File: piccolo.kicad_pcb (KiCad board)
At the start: 2 copper layers, 21 x 51 mm, 44 parts, among them J0 CON_PICO_40W, J1 USB_C_Receptacle_USB2.0, J2 Debug, Q1 DMG1012T, SW1 BOOTSEL, U1 RP2040, U2 ME6217C33M5, U3 MX25R1635FZUIL0, X1 SIT1602AI-22-33E-12.000000D

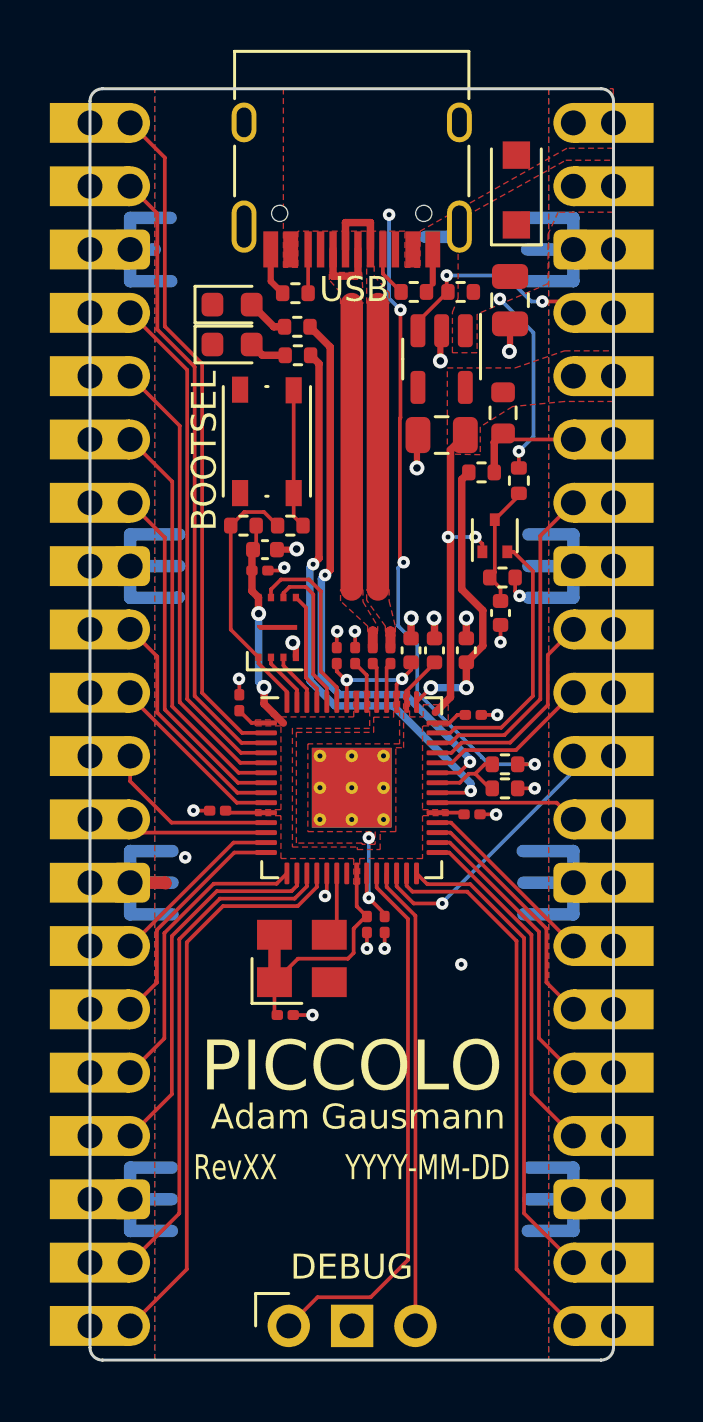
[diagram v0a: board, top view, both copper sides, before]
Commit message: value-engineered for jlcpcb
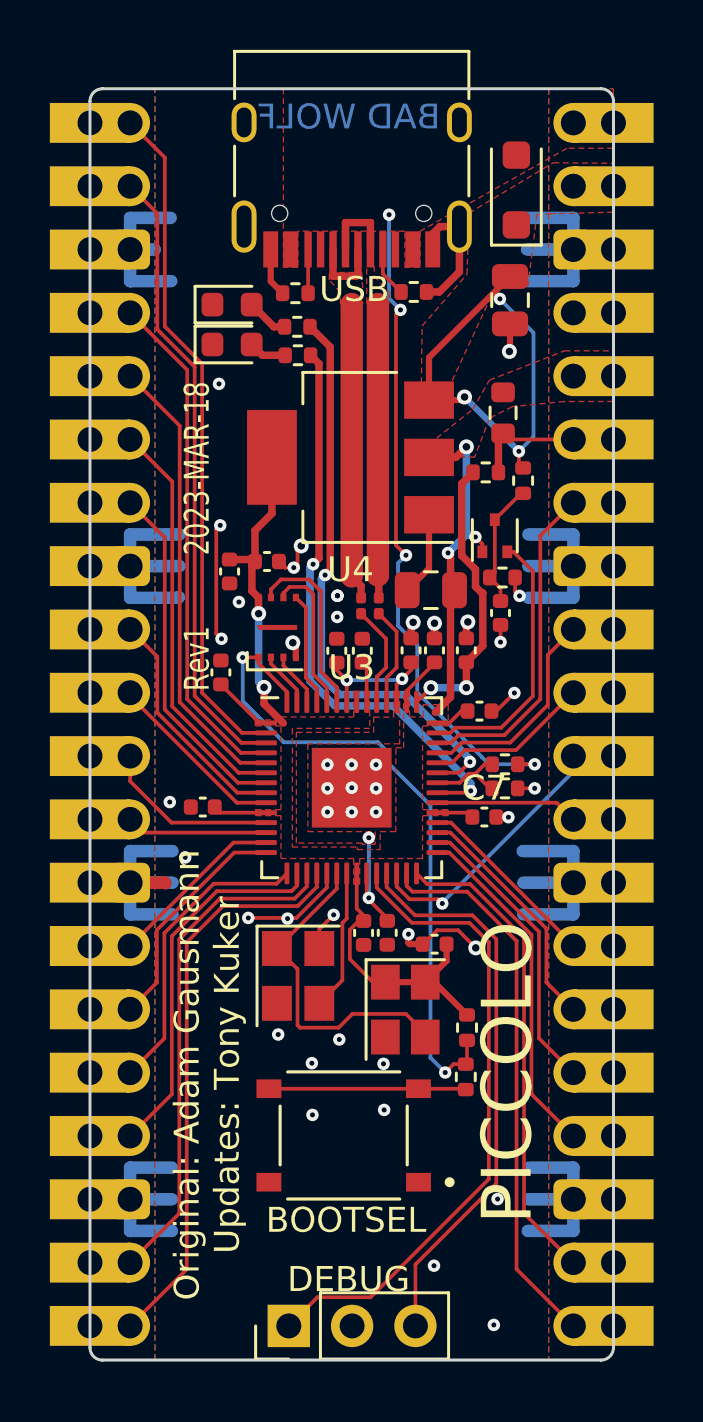
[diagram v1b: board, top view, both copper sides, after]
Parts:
- removed the R2 at (126.0, 48.4)
- removed SW1: BOOTSEL, Button_Switch_SMD:SW_Push_1P1T_NO_Vertical_Wuerth_434133025816
- removed U2: ME6217C33M5, Package_TO_SOT_SMD:SOT-23-5
- added SW2: TS-1187A-B-A-B, TS-1187A-B-A-B:SW_TS-1187A-B-A-B, F.Cu at (121.3, 82.2)
- added U4: AMS1117-3.3, Package_TO_SOT_SMD:SOT-223-3_TabPin2, F.Cu at (121.5, 55.0)
- added Y1: 12MHz, Crystal:Crystal_SMD_3225-4Pin_3.2x2.5mm, F.Cu at (119.5, 75.8)
- C10: renamed from C8; footprint Capacitor_SMD:C_0201_0603Metric -> Capacitor_SMD:C_0402_1005Metric
- C11: renamed from C10; footprint Capacitor_SMD:C_0201_0603Metric -> Capacitor_SMD:C_0402_1005Metric
- C13: renamed from C9; footprint Capacitor_SMD:C_0201_0603Metric -> Capacitor_SMD:C_0402_1005Metric
- C15: renamed from C11; footprint Capacitor_SMD:C_0201_0603Metric -> Capacitor_SMD:C_0402_1005Metric
- C17: renamed from C16; footprint Capacitor_SMD:C_0201_0603Metric -> Capacitor_SMD:C_0402_1005Metric
- C2: renamed from C15; footprint Capacitor_SMD:C_0201_0603Metric -> Capacitor_SMD:C_0402_1005Metric
- C5: renamed from C4; footprint Capacitor_SMD:C_0201_0603Metric -> Capacitor_SMD:C_0402_1005Metric
- C7: renamed from C6; footprint Capacitor_SMD:C_0201_0603Metric -> Capacitor_SMD:C_0402_1005Metric
- C8: renamed from C5; footprint Capacitor_SMD:C_0201_0603Metric -> Capacitor_SMD:C_0402_1005Metric
- C9: renamed from C7; footprint Capacitor_SMD:C_0201_0603Metric -> Capacitor_SMD:C_0402_1005Metric
- D3: value Yellow -> Red
- U1: renamed from U3; value MX25R1635FZUIL0 -> W25Q16JVUXIQ
- U3: renamed from U1; footprint agausmann:RP2040_QFN-56-1EP_7x7mm_P0.4mm_EP3.2x3.2mm_ThermalVias -> Package_DFN_QFN:QFN-56-1EP_7x7mm_P0.4mm_EP3.2x3.2mm
- X1: value SIT1602AI-22-33E-12.000000D -> SIT1602AI-22-33E-12.000000; footprint agausmann:SiT1602xx-2_3.2x2.5mm -> Crystal:Crystal_SMD_SeikoEpson_TSX3225-4Pin_3.2x2.5mm
- moved R2 23.2 mm to (126.2, 79.8), turned to -90 degrees
- moved R1 22.0 mm to (126.2, 77.9), turned to -90 degrees
- moved C17 6.63 mm to (124.9, 74.5), turned to 180 degrees
- moved C6 6.24 mm to (124.8, 60.3)
- moved X1 4.63 mm to (123.8, 77.1), turned to -90 degrees
- moved R10 2.05 mm to (122.0, 60.9)
- moved R11 2.05 mm to (122.7, 60.9)
- moved C1 1.67 mm to (116.7, 59.6), turned to -90 degrees
- moved C5 1.42 mm to (116.3, 63.6)
- moved C8 0.61 mm to (115.6, 69.0)
- moved C7 0.51 mm to (126.9, 69.4)
- moved C2 0.46 mm to (118.2, 59.2)
- moved C10 0.36 mm to (122.1, 74.1)
- moved C13 0.35 mm to (123.0, 74.1)
- moved C11 0.35 mm to (122.0, 62.7)
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- renumbered C18 to C1, C14 to C12, C12 to C14, C13 to C16, C1 to C4, C2 to C6, J0 to J2, J2 to J3, R4 to R1, R12 to R10, R13 to R11, R7 to R12, R9 to R13, R3 to R14, R8 to R15, R11 to R2, R16 to R3, R17 to R4, R10 to R5, R1 to R6, R5 to R7, R6 to R8
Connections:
- U3 pad 21: unconnected-(U1-Pad21) -> /XOUT
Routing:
- net /QSPI_SS: track 10.3 -> 27.0 mm, vias 0 -> 2
- net GND: track 87.0 -> 98.6 mm, vias 24 -> 44
- net /VSYS: track 7.58 -> 18.4 mm, vias 2 -> 3
- net /XIN: track 2.59 -> 13.4 mm
- net +3V3: track 41.6 -> 50.1 mm, vias 4 -> 5
- net /3V3_EN: track 8.44 -> 0.00 mm, vias 2 -> 0
- net /XOUT: track 0.00 -> 5.67 mm
- net /SWDIO: track 18.6 -> 22.7 mm
- net /SWCLK: track 21.9 -> 25.9 mm
- net Net-(U3-USB_DP): track 1.61 -> 4.11 mm
- net Net-(U3-USB_DM): track 1.61 -> 4.00 mm
- net Net-(R2-Pad2): track 5.58 -> 7.76 mm
- net /ADC_VREF: track 4.63 -> 3.95 mm
- net /RUN: track 10.7 -> 10.1 mm
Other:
- board text added: "2023-MAR-18"
- board text added: "BAD WOLF"
- board text added: "Original: Adam Gausmann Updates: Tony Kuker"
- board text added: "Rev1"
- board text removed: "Adam Gausmann"
- board text removed: "RevXX"
- board text removed: "YYYY-MM-DD"
